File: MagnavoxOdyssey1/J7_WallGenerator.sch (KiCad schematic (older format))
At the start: 19 parts

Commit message: mais outro pedação do circuito transcrito :-)
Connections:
- net (8) renamed (8)_NC
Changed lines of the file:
@@
 LIBS:valves
 LIBS:ferrite
+LIBS:conn_22x2
 LIBS:MagnavoxOdyssey1-cache
 EELAYER 25 0
@@
 $Descr A4 11693 8268
 encoding utf-8
-Sheet 4 5
+Sheet 4 7
 Title ""
 Date ""
@@
 $EndComp
 $Comp
-L GND #PWR020
+L GND #PWR023
 U 1 1 588DCD18
 P 5600 2900
-F 0 "#PWR020" H 5600 2900 30  0001 C CNN
+F 0 "#PWR023" H 5600 2900 30  0001 C CNN
 F 1 "GND" H 5600 2830 30  0001 C CNN
 F 2 "" H 5600 2900 60  0001 C CNN
@@
 $EndComp
 $Comp
-L GND #PWR021
+L GND #PWR024
 U 1 1 588DCE8C
 P 7950 2900
-F 0 "#PWR021" H 7950 2900 30  0001 C CNN
+F 0 "#PWR024" H 7950 2900 30  0001 C CNN
 F 1 "GND" H 7950 2830 30  0001 C CNN
 F 2 "" H 7950 2900 60  0001 C CNN
@@
 $EndComp
 $Comp
-L GND #PWR022
+L GND #PWR025
 U 1 1 588DD5E8
 P 5600 4800
-F 0 "#PWR022" H 5600 4800 30  0001 C CNN
+F 0 "#PWR025" H 5600 4800 30  0001 C CNN
 F 1 "GND" H 5600 4730 30  0001 C CNN
 F 2 "" H 5600 4800 60  0001 C CNN
@@
 $EndComp
 $Comp
-L GND #PWR023
+L GND #PWR026
 U 1 1 588DDF40
 P 7950 4600
-F 0 "#PWR023" H 7950 4600 30  0001 C CNN
+F 0 "#PWR026" H 7950 4600 30  0001 C CNN
 F 1 "GND" H 7950 4530 30  0001 C CNN
 F 2 "" H 7950 4600 60  0001 C CNN
@@
 	7550 3300 7850 3300
 Text HLabel 8900 3600 2    60   Output ~ 0
-(8)
+(8)_NC
 Text HLabel 8950 2000 2    60   Output ~ 0
 (7)

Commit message: mais um pedação
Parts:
- 7_C3: value 45 -> .15
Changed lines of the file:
@@
 $Descr A4 11693 8268
 encoding utf-8
-Sheet 4 9
+Sheet 4 10
 Title ""
 Date ""
@@
 P 4950 4750
 F 0 "7_C3" H 5083 4796 50  0000 L CNN
-F 1 "45" H 5083 4705 50  0000 L CNN
+F 1 ".15" H 5083 4705 50  0000 L CNN
 F 2 "" H 4950 4750 60  0000 C CNN
 F 3 "" H 4950 4750 60  0000 C CNN

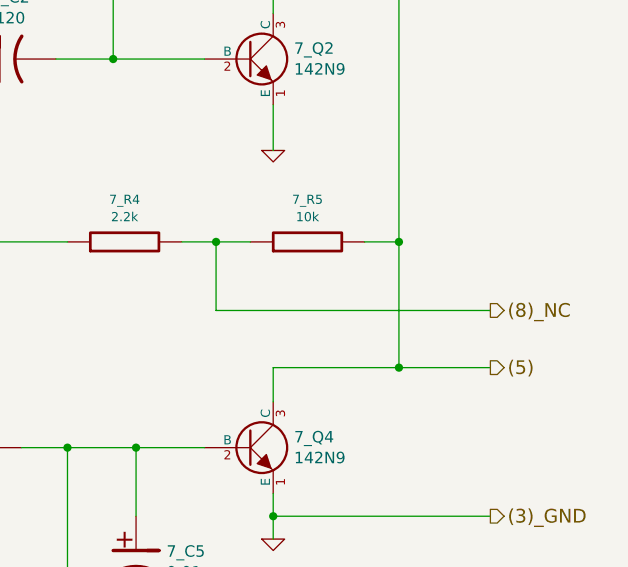
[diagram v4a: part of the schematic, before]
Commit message: terminei de transcrever a PCB toda. Deixei de fora de propósito o estágio de modulação RF do sinal. É pouca coisa, posso adicionar amanhã ou depois... Gerei também um PDFão
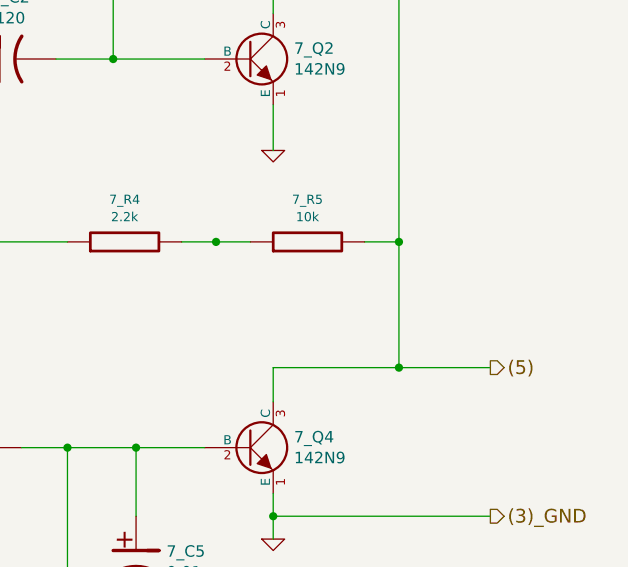
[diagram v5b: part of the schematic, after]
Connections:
- net (8)_NC: no longer names the net of 7_R4.2, 7_R5.1
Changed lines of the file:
@@
 $Descr A4 11693 8268
 encoding utf-8
-Sheet 4 11
+Sheet 4 12
 Title ""
 Date ""
@@
 $EndComp
 $Comp
-L GND #PWR023
+L GND #PWR053
 U 1 1 588DCD18
 P 5600 2900
-F 0 "#PWR023" H 5600 2900 30  0001 C CNN
+F 0 "#PWR053" H 5600 2900 30  0001 C CNN
 F 1 "GND" H 5600 2830 30  0001 C CNN
 F 2 "" H 5600 2900 60  0001 C CNN
@@
 $EndComp
 $Comp
-L GND #PWR024
+L GND #PWR054
 U 1 1 588DCE8C
 P 7950 2900
-F 0 "#PWR024" H 7950 2900 30  0001 C CNN
+F 0 "#PWR054" H 7950 2900 30  0001 C CNN
 F 1 "GND" H 7950 2830 30  0001 C CNN
 F 2 "" H 7950 2900 60  0001 C CNN
@@
 $EndComp
 $Comp
-L GND #PWR025
+L GND #PWR055
 U 1 1 588DD5E8
 P 5600 4800
-F 0 "#PWR025" H 5600 4800 30  0001 C CNN
+F 0 "#PWR055" H 5600 4800 30  0001 C CNN
 F 1 "GND" H 5600 4730 30  0001 C CNN
 F 2 "" H 5600 4800 60  0001 C CNN
@@
 $EndComp
 $Comp
-L GND #PWR026
+L GND #PWR056
 U 1 1 588DDF40
 P 7950 4600
-F 0 "#PWR026" H 7950 4600 30  0001 C CNN
+F 0 "#PWR056" H 7950 4600 30  0001 C CNN
 F 1 "GND" H 7950 4530 30  0001 C CNN
 F 2 "" H 7950 4600 60  0001 C CNN
@@
 Wire Wire Line
 	7550 3300 7850 3300
-Text HLabel 8900 3600 2    60   Output ~ 0
-(8)_NC
 Text HLabel 8950 2000 2    60   Output ~ 0
 (7)
-Wire Wire Line
-	8900 3600 7700 3600
-Wire Wire Line
-	7700 3600 7700 3300
-Connection ~ 7700 3300
 Wire Wire Line
 	8950 2000 7250 2000
@@
 	3350 5150 3100 5150
 Connection ~ 4950 5150
+Connection ~ 7700 3300
 $EndSCHEMATC
